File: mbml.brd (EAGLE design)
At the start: 69.8 x 57.1 mm, 16 parts, among them IC1 MAX392CPE, J1 CON-2B2B-XH-A(LF)(SN), J2 CON-2B2B-XH-A(LF)(SN), K1 G5SB, Q1 2N2222, X1 43160-1102

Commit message: Finished board
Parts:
- removed IC1: MAX392CPE, maxim:DIL16
- added OK1: ILQ1, optocoupler:DIL16
- added R1, R2, R3, R6: 470, resistor:0204/5
- added R4, R5: 10k, resistor:0204/5
- added X8: CON-2B2B-XH-A(LF)(SN), FVP:CON_2-2.5MM_TH
- renumbered J1 to X3, J2 to X4, U$2 to X5, U$3 to X6, U$4 to X7, U$5 to X2
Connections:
- removed net V+: IC1.13
- removed net V-: IC1.4
- new net N$15: OK1.15, X7.P$1
- new net N$16: OK1.16, X7.P$2
- new net N$17: OK1.8, R6.1
- new net N$18: R6.2, U$1.9
- new net N$19: OK1.10, X8.P$1
- new net N$20: OK1.9, X8.P$2
- new net N$7: OK1.4, R2.1
- net GND: now also OK1.2, OK1.3, OK1.6, OK1.7, R4.2, R5.2; no longer IC1.5
- net N$1: now also R4.1
- net N$10: now also R3.2; no longer IC1.1
- net N$11: now also OK1.11, X5.P$1; no longer IC1.11, X7.P$2
- net N$12: now also OK1.12, X5.P$2; no longer IC1.10, X7.P$1
- net N$13: now also OK1.14; no longer IC1.15
- net N$14: now also OK1.13, X6.P$2; no longer IC1.2, X5.P$1
- net N$2: now also R5.1
- net N$4: now also R1.2; no longer IC1.9
- net N$5: now also U$1.10; no longer U$1.9
- net N$6: now also OK1.5, R3.1; no longer IC1.3, X5.P$2
- net N$8: now also OK1.1, R1.1; no longer IC1.14, X6.P$2
- net N$9: now also R2.2; no longer IC1.16
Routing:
- net N$19: track 0.00 -> 28.6 mm
- net N$4: track 32.3 -> 4.03 mm
- net N$20: track 0.00 -> 27.9 mm
- net N$15: track 0.00 -> 22.4 mm
- net N$45: track 0.00 -> 22.0 mm, vias 0 -> 1
- net N$43: track 0.00 -> 22.0 mm, vias 0 -> 1
- net N$41: track 0.00 -> 22.0 mm, vias 0 -> 1
- net N$34: track 0.00 -> 22.0 mm, vias 0 -> 1
- net N$42: track 0.00 -> 22.0 mm, vias 0 -> 1
- net N$40: track 0.00 -> 21.9 mm, vias 0 -> 1
- net N$37: track 0.00 -> 21.9 mm, vias 0 -> 1
- net N$44: track 0.00 -> 21.9 mm, vias 0 -> 1
- net N$39: track 0.00 -> 21.6 mm, vias 0 -> 1
- net N$38: track 0.00 -> 21.5 mm, vias 0 -> 1
- net N$7: track 0.00 -> 20.9 mm
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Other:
- board text added: "+12V IN"
- board text added: "+5V"
- board text added: "10"
- board text added: "11"
- board text added: "12"
- board text added: "13"
- board text added: "3"
- board text added: "4"
- board text added: "5"
- board text added: "6"
- board text added: "8"
- board text added: "9"
- board text added: "A0"
- board text added: "A1"
- board text added: "A2"
- board text added: "A3"
- board text added: "A4"
- board text added: "A5"
- board text added: "AUX SW"
- board text added: "Aref"
- board text added: "BAT"
- board text added: "BUS"
- board text added: "CPU SW"
- board text added: "FULL VIEW PRODUCTIONS"
- board text added: "GND"
- board text added: "MAIN BTN"
- board text added: "MBML1 CONTROL BOARD"
- board text added: "MONITOR PWR"
- board text added: "PROJ BTN"
- board text added: "PROJ SW"
- board text added: "RST"
- board text added: "RX"
- board text added: "SPKR SW"
- board text added: "TX"
- board text added: "X2"
- board text added: "~"

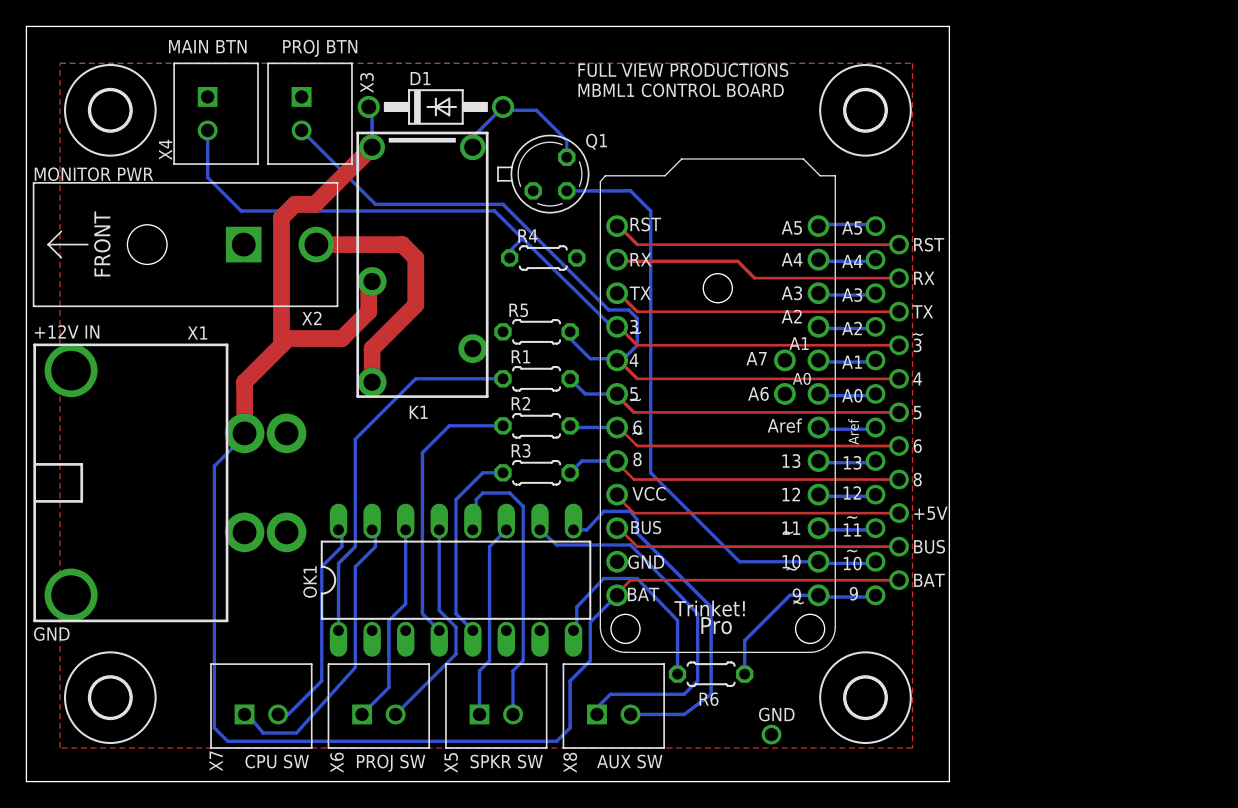
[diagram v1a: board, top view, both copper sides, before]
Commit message: Version 2.0 Changes
Added:
- 5V regulator
- Speaker power connector
- Fan power connector
- Fan power photocoupler

Fixed:
- Missing monitor relay transistor base current limiting resistor
- Changed power button resistors from pull down to pull up
- Increased spacing between MCU pin holes to allow for installation of
female headers
- Added more GND test vias
- Added +12V and +5V test via
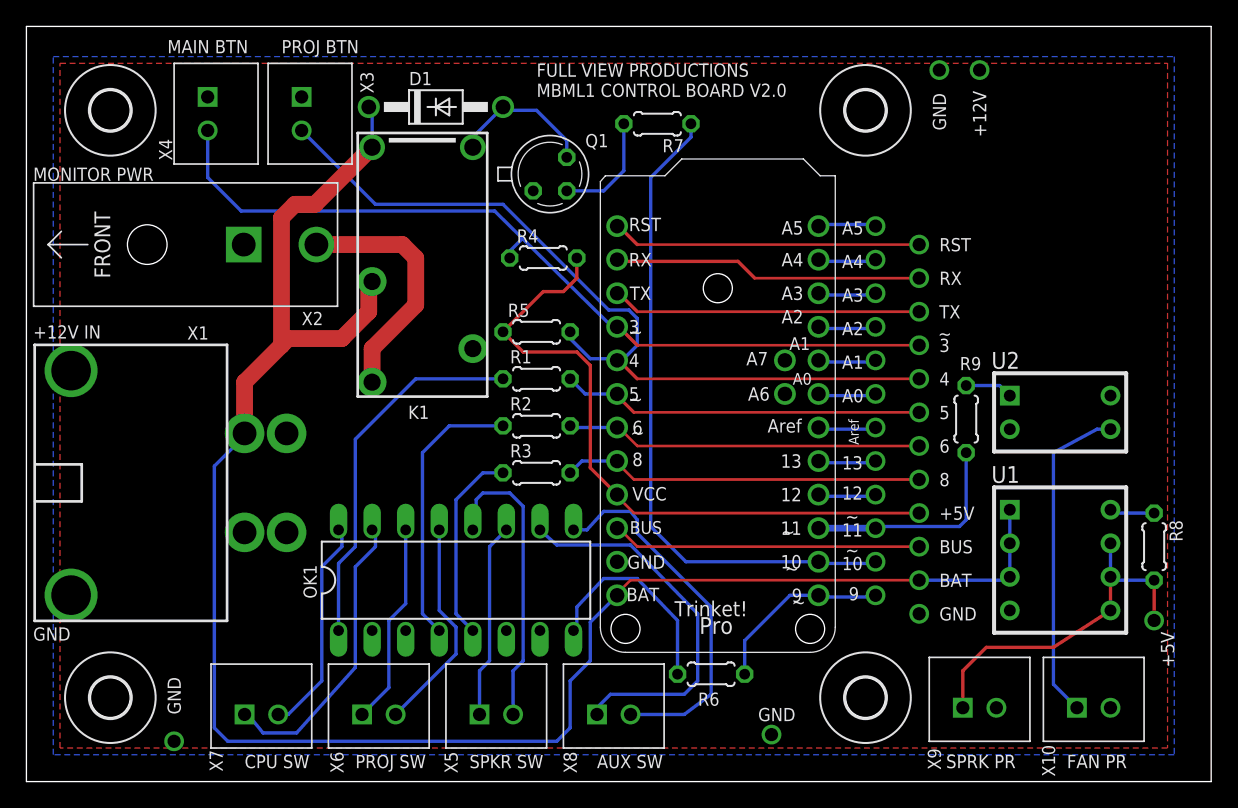
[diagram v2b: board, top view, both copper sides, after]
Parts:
- added R7: 1.54k, resistor:0204/5
- added R8: 250k, resistor:0204/5
- added R9: 470, resistor:0204/5
- added U1: LINEAR_REG_5V, TinkerTech:DIP-8
- added U2: PHOTOCOUPLER, TinkerTech:DIP-4
- added X10, X9: CON-2B2B-XH-A(LF)(SN), FVP:CON_2-2.5MM_TH
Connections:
- removed net VCC: U$1.VCC
- new net +5V: R8.2, U1.5, U1.6, U1.7, X9.P$1
- new net MCU_VCC: R4.2, R5.2, U$1.VCC
- new net N$35: R7.1, U$1.10
- new net N$46: R9.1, U2.1
- new net N$47: R9.2, U$1.11
- new net N$48: R8.1, U1.8
- new net N$49: U2.3, X10.P$1
- net +12V: now also U1.1, U1.2, U1.3, U2.4
- net GND: now also U1.4, U2.2, X10.P$2, X9.P$2; no longer R4.2, R5.2
- net N$5: now also R7.2; no longer U$1.10
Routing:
- net N$35: track 0.00 -> 45.5 mm
- net N$5: track 42.3 -> 8.51 mm
- net MCU_VCC: track 0.00 -> 27.1 mm
- net +5V: track 0.00 -> 27.1 mm, vias 0 -> 1
- net N$49: track 0.00 -> 24.8 mm
- net N$47: track 0.00 -> 16.5 mm
- net +12V: track 124.3 -> 138.2 mm, vias 1 -> 2
- net N$46: track 0.00 -> 3.62 mm
- net N$48: track 0.00 -> 3.41 mm
- net N$45: track 22.0 -> 23.5 mm
- net N$44: track 21.9 -> 23.4 mm
- net N$43: track 22.0 -> 23.5 mm
- net N$42: track 22.0 -> 23.5 mm
- net N$41: track 22.0 -> 23.5 mm
- net N$40: track 21.9 -> 23.4 mm
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- added copper zone on layer 16, net +12V
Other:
- board size 69.8 x 57.1 mm -> 89.7 x 57.1 mm
- board text added: "+12V"
- board text added: "FAN PR"
- board text added: "MBML1 CONTROL BOARD V2.0"
- board text added: "SPRK PR"
- board text removed: "MBML1 CONTROL BOARD"
